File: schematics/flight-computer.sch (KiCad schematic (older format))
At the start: 45 parts, among them IC1 NC7SZ04, IC2 MAX14787E, IC3 MAX14787E, J1 BATT, J2 SERIAL, J3 BLACKBOX, P1 SWD_TC, P2 GPS, P3 TLM, U1 MAX604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

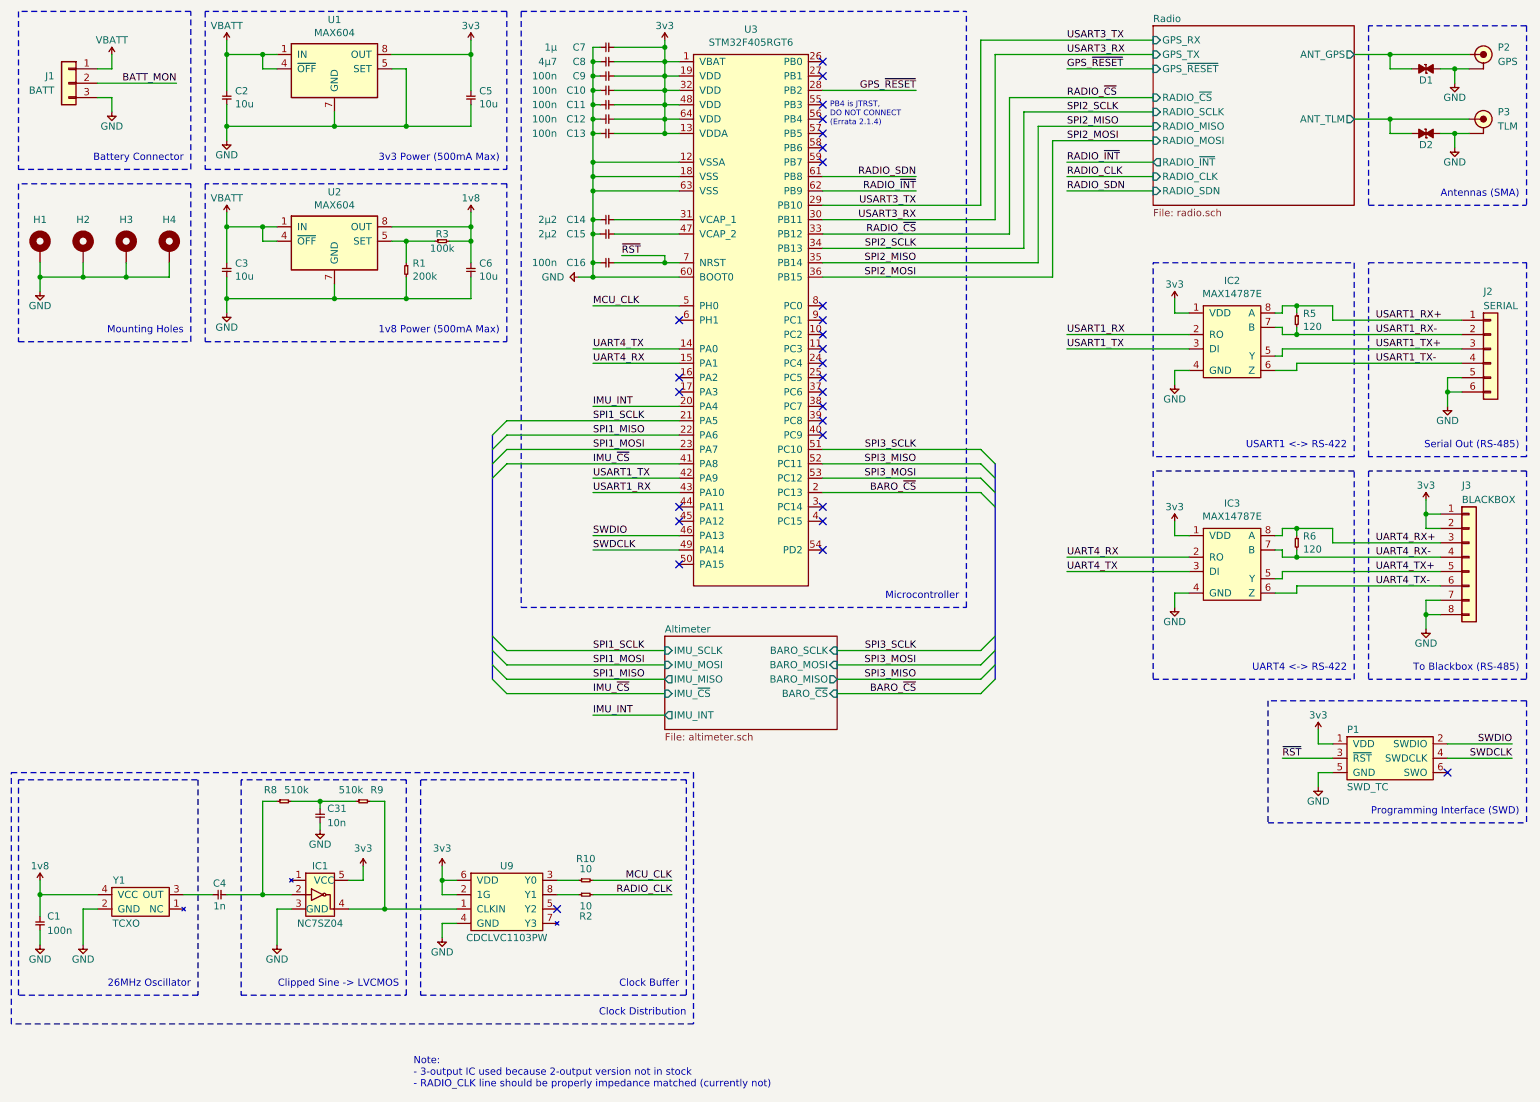
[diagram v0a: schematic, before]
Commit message: Migrate remaining symbols to local library
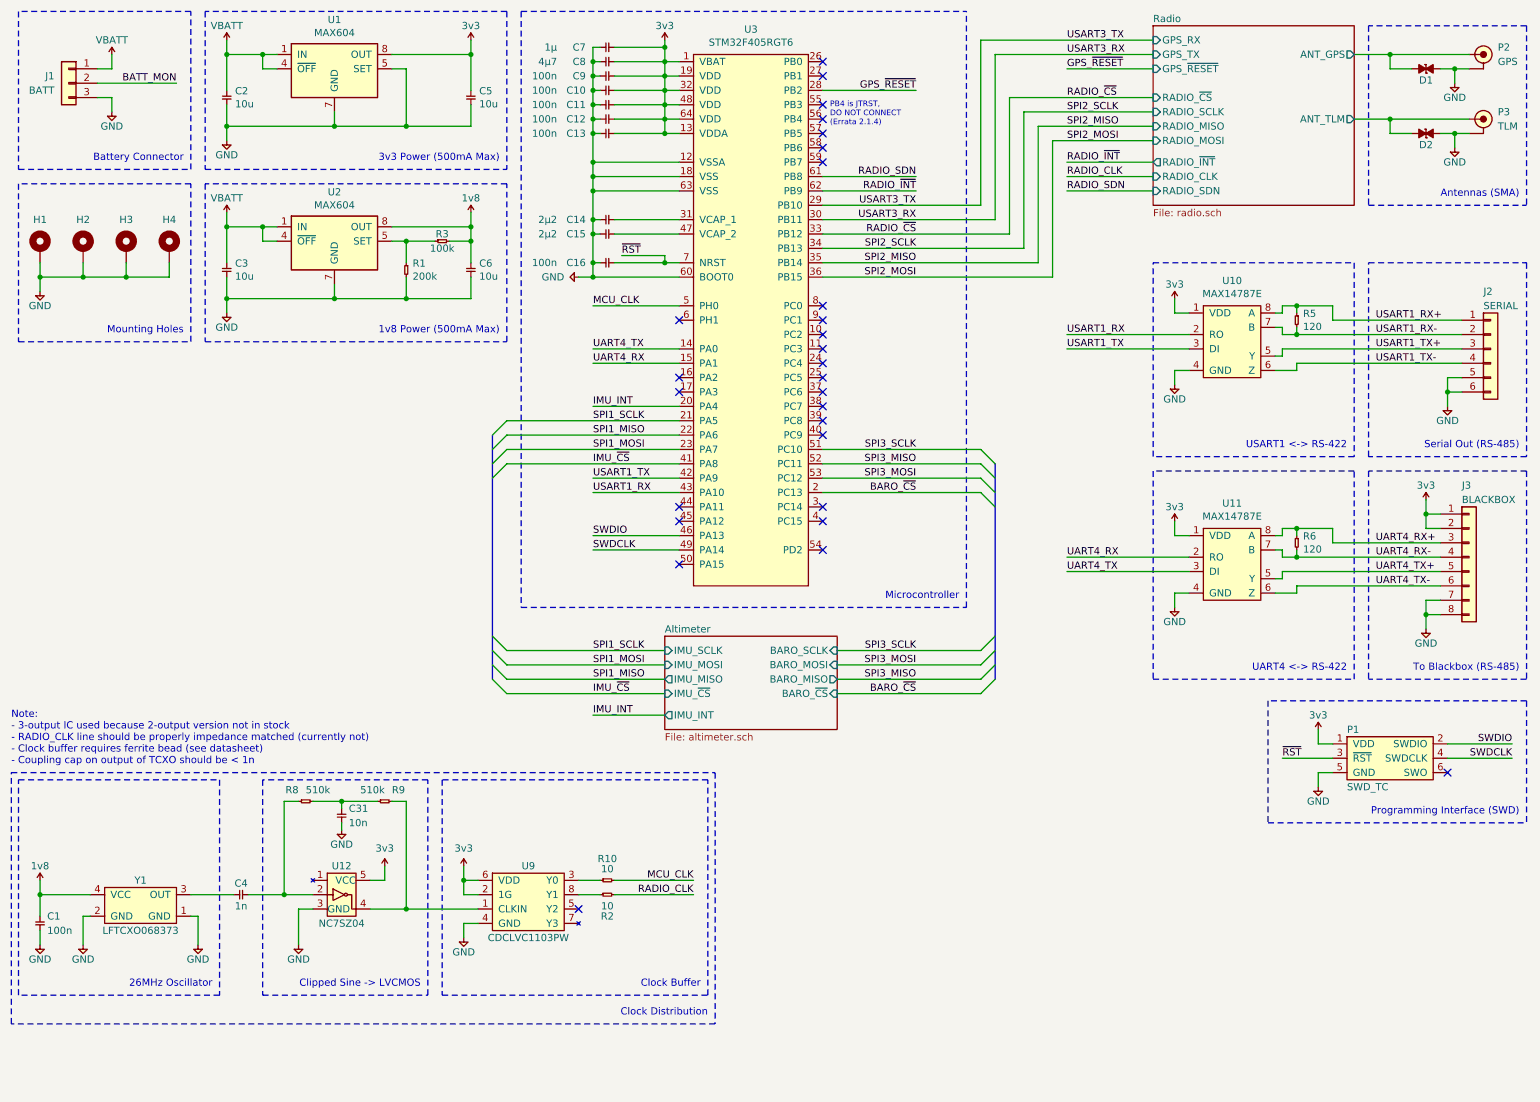
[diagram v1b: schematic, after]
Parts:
- removed Y1: TCXO, cusf:XTAL-25x20, symbol Strix:TCXO
- added Y1: LFTCXO068373, Strix:LFTCXO068373, symbol Strix:LFTCXO068373
- C1, C10, C11, C12, C13, C14, C15, C16, C2, C3, C31, C4, C5, C6, C7, C8, C9: footprint Strix:C_0402_1005Metric_Pad0.74x0.62mm_HandSolder -> Strix:C_0402
- D1, D2: footprint Strix:D_0402_1005Metric_Pad0.77x0.64mm_HandSolder -> Strix:D_0402
- H1, H2, H3, H4: footprint Strix:MountingHole_3.2mm_M3_Pad_Via -> Strix:MountingHole_Pad
- J1: footprint Strix:Molex_Nano-Fit_105313-xx03_1x03_P2.50mm_Horizontal -> Strix:Molex_Nano-Fit_105313-1103
- J2: footprint Strix:Molex_Nano-Fit_105314-xx06_2x03_P2.50mm_Horizontal -> Strix:Molex_Nano-Fit_105314-1106
- J3: footprint Strix:Molex_Nano-Fit_105314-xx08_2x04_P2.50mm_Horizontal -> Strix:Molex_Nano-Fit_105314-1108
- P1: footprint Strix:Tag-Connect_TC2030-IDC-NL_2x03_P1.27mm_Vertical -> Strix:SWD_TC
- R1, R10, R2, R3, R5, R6, R8, R9: footprint Strix:R_0402_1005Metric_Pad0.72x0.64mm_HandSolder -> Strix:R_0402
- U1, U2: footprint Strix:SOIC-8_3.9x4.9mm_P1.27mm -> Strix:MAX604
- U3: footprint Strix:LQFP-64_10x10mm_P0.5mm -> Strix:STM32F405RGT6
- U9: footprint Strix:TSSOP-8_4.4x3mm_P0.65mm -> Strix:CDCLVC1103PW
- renumbered IC2 to U10, IC3 to U11, IC1 to U12
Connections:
- net 1v8: now also Y1.4 (VCC)
- net GND: now also Y1.1 (GND), Y1.2 (GND)
- net at C4.1: now also Y1.3 (OUT)
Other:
- note added: "Note:\n- 3-output IC used because 2-output version not in stock\n- RADIO_CLK line should be properly impedance matched (currently not)\n- Clock buffer requires ferrite bead (see datasheet)\n- Coupling cap on output of TCXO should be < 1n"
- note removed: "Note:\n- 3-output IC used because 2-output version not in stock\n- RADIO_CLK line should be properly impedance matched (currently not)"
- moved on the sheet: C31, C4, R10, R2, R8, R9, U12, U9

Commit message: Misc fixes
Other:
- note added: "1v8 Power (300mA Max)"
- note added: "3v3 Power (300mA Max)"
- note removed: "1v8 Power (500mA Max)"
- note removed: "3v3 Power (500mA Max)"
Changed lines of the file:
@@
 $EndComp
 Text Notes 3950 1700 2    50   ~ 0
-3v3 Power (500mA Max)
+3v3 Power (300mA Max)
 Wire Notes Line
 	4000 650  1900 650
@@
 $EndComp
 Text Notes 3950 2900 2    50   ~ 0
-1v8 Power (500mA Max)
+1v8 Power (300mA Max)
 Wire Notes Line
 	4000 2950 4000 1850
@@
 Wire Wire Line
 	4000 5400 5100 5400
-Wire Bus Line
-	3900 3600 3900 5300
-Wire Bus Line
-	7400 3800 7400 5300
 $Comp
 L Strix:LFTCXO068373 Y1
@@
 	1    0    0    -1
 $EndComp
+Wire Bus Line
+	3900 3600 3900 5300
+Wire Bus Line
+	7400 3800 7400 5300
 $EndSCHEMATC
